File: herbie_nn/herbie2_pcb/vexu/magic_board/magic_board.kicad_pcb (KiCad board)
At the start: 2 copper layers, 70 x 50 mm, 65 parts, among them J1 4P4C, J2 Conn_ARM_JTAG_SWD_10, J3 USB_C_Receptacle_USB2.0_14P, J4 Conn_01x04_Pin, J5 Conn_01x04_Pin, U10 SN74LVC245APW, U11 74HC14, U2 AT25SF081-SSHD-X, U3 BD33FC0WEFJ, U4 ATSAMD51J19A-A, U5 LS7366R, U6 LS7366R, U7 LS7366R, U8 LS7366R, U9 SN74LVC245APW, Y1 32.768KHz, Y2 20MHz

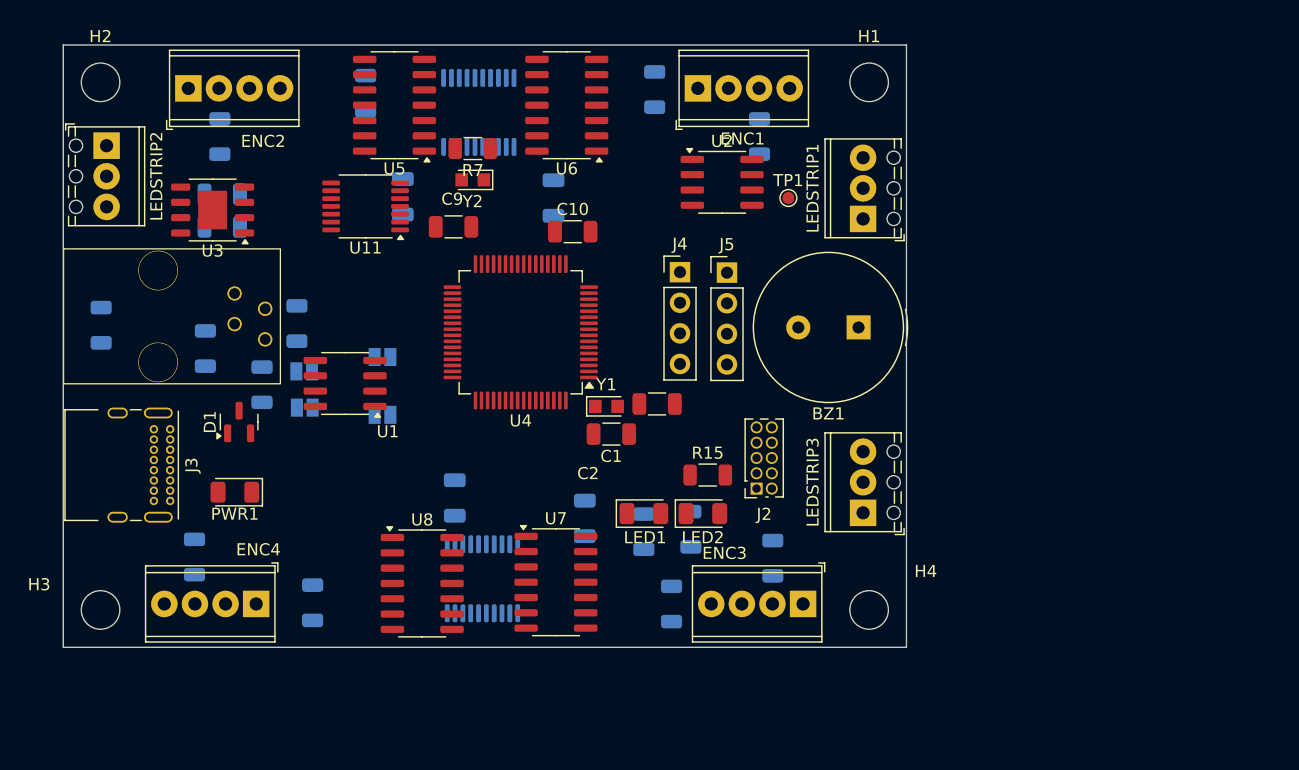
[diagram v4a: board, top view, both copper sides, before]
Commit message: change regulator
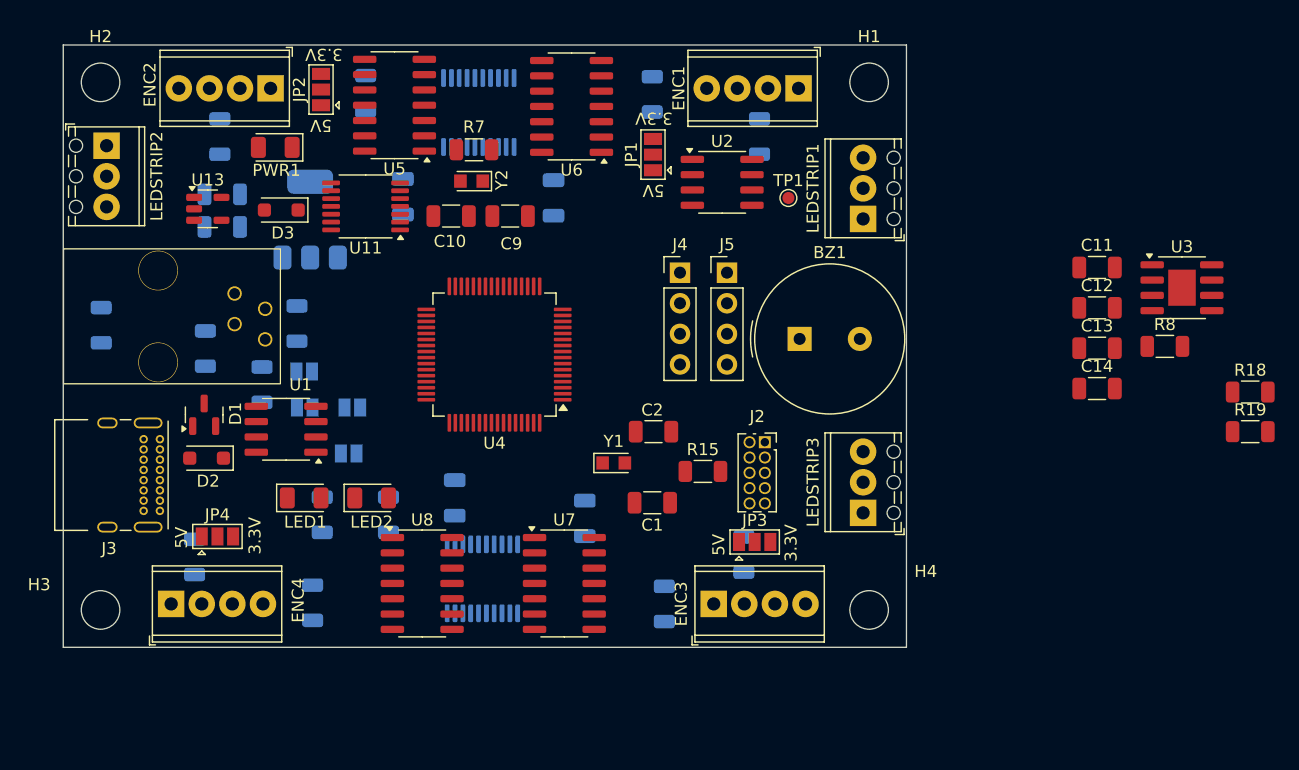
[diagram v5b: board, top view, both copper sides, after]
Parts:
- added C11: C, Capacitor_SMD:C_1206_3216Metric, F.Cu at (111.3, 80.5)
- added C12: C, Capacitor_SMD:C_1206_3216Metric, F.Cu at (111.3, 83.8)
- added C13: C, Capacitor_SMD:C_1206_3216Metric, F.Cu at (111.3, 87.2)
- added C14: C, Capacitor_SMD:C_1206_3216Metric, F.Cu at (111.3, 90.5)
- added D2: MBR1020VL, Diode_SMD:D_SOD-123F, F.Cu at (37.4, 96.3)
- added D3: MBR1020VL, Diode_SMD:D_SOD-123F, F.Cu at (43.6, 75.7)
- added JP1: SolderJumper_3_Open, Jumper:SolderJumper-3_P1.3mm_Open_Pad1.0x1.5mm, F.Cu at (74.5, 71.1)
- added JP2: SolderJumper_3_Open, Jumper:SolderJumper-3_P1.3mm_Open_Pad1.0x1.5mm, F.Cu at (46.9, 65.7)
- added JP3: SolderJumper_3_Open, Jumper:SolderJumper-3_P1.3mm_Open_Pad1.0x1.5mm, F.Cu at (82.9, 103.3)
- added JP4: SolderJumper_3_Open, Jumper:SolderJumper-3_P1.3mm_Open_Pad1.0x1.5mm, F.Cu at (38.3, 102.8)
- added R18: R, Resistor_SMD:R_1206_3216Metric, F.Cu at (124.0, 90.8)
- added R19: R, Resistor_SMD:R_1206_3216Metric, F.Cu at (124.0, 94.1)
- added R8: R, Resistor_SMD:R_1206_3216Metric, F.Cu at (117.0, 87.0)
- added U12: AMS1117-5.0, Package_TO_SOT_SMD:SOT-223-3_TabPin2, B.Cu at (46.0, 76.5)
- added U13: AP2112K-3.3, Package_TO_SOT_SMD:SOT-23-5, F.Cu at (37.5, 75.6)
- U3: value BD33FC0WEFJ -> LM386; footprint Package_SO:HTSOP-8-1EP_3.9x4.9mm_P1.27mm_EP2.4x3.2mm -> Package_SO:SOIC-8-1EP_3.9x4.9mm_P1.27mm_EP2.29x3mm
- Y2: value 20MHz -> 8MHz
- moved U3 80.7 mm to (118.4, 82.2), turned to 0 degrees
- moved PWR1 28.8 mm to (43.1, 70.5)
- moved LED1 28.2 mm to (45.5, 99.6)
- moved LED2 27.5 mm to (51.1, 99.6)
- moved R4 26.7 mm to (47.0, 101.0)
- moved R5 25.1 mm to (52.5, 101.0)
- moved C10 10.2 mm to (57.7, 76.2)
- moved ENC1 8.36 mm to (86.5, 65.6), turned to 180 degrees
- moved ENC3 7.42 mm to (79.5, 108.4), turned to 0 degrees
- moved ENC4 7.05 mm to (34.5, 108.4), turned to 0 degrees
- moved ENC2 6.83 mm to (42.7, 65.6), turned to 180 degrees
- moved C1 6.64 mm to (74.4, 100.0)
- moved U1 6.20 mm to (44.0, 93.9)
- moved BZ1 4.98 mm to (86.6, 86.4), turned to 0 degrees
- moved JP_TX1 4.89 mm to (49.5, 92.1), turned to 180 degrees
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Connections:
- ENC1 pad 4: unconnected-(ENC1-Pin_4-Pad4) -> Net-(ENC1-Pin_4)
- ENC2 pad 4: unconnected-(ENC2-Pin_4-Pad4) -> Net-(ENC2-Pin_4)
- ENC3 pad 4: unconnected-(ENC3-Pin_4-Pad4) -> Net-(ENC3-Pin_4)
- ENC4 pad 4: unconnected-(ENC4-Pin_4-Pad4) -> Net-(ENC4-Pin_4)
- R3 pad 1: +12V -> +5V
- U3 pad 1: +3.3V -> Net-(C13-Pad1)
- U3 pad 2: unconnected-(U3-NC-Pad2) -> GND
- U3 pad 3: GND -> Net-(U3-+)
- U3 pad 4: unconnected-(U3-NC-Pad4) -> GND
- U3 pad 5: +12V -> Net-(C11-Pad1)
- U3 pad 6: unconnected-(U3-NC-Pad6) -> +5V
- U3 pad 8: +12V -> Net-(C13-Pad2)
- U3 pad 9: GND -> (no net)
- U9 pad 1: unconnected-(U9-DIR-Pad1) -> +3.3V
- U9 pad 19: unconnected-(U9-~{OE}-Pad19) -> GND
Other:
- board text added: "3.3V"
- board text added: "5V"

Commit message: updated encoder chip
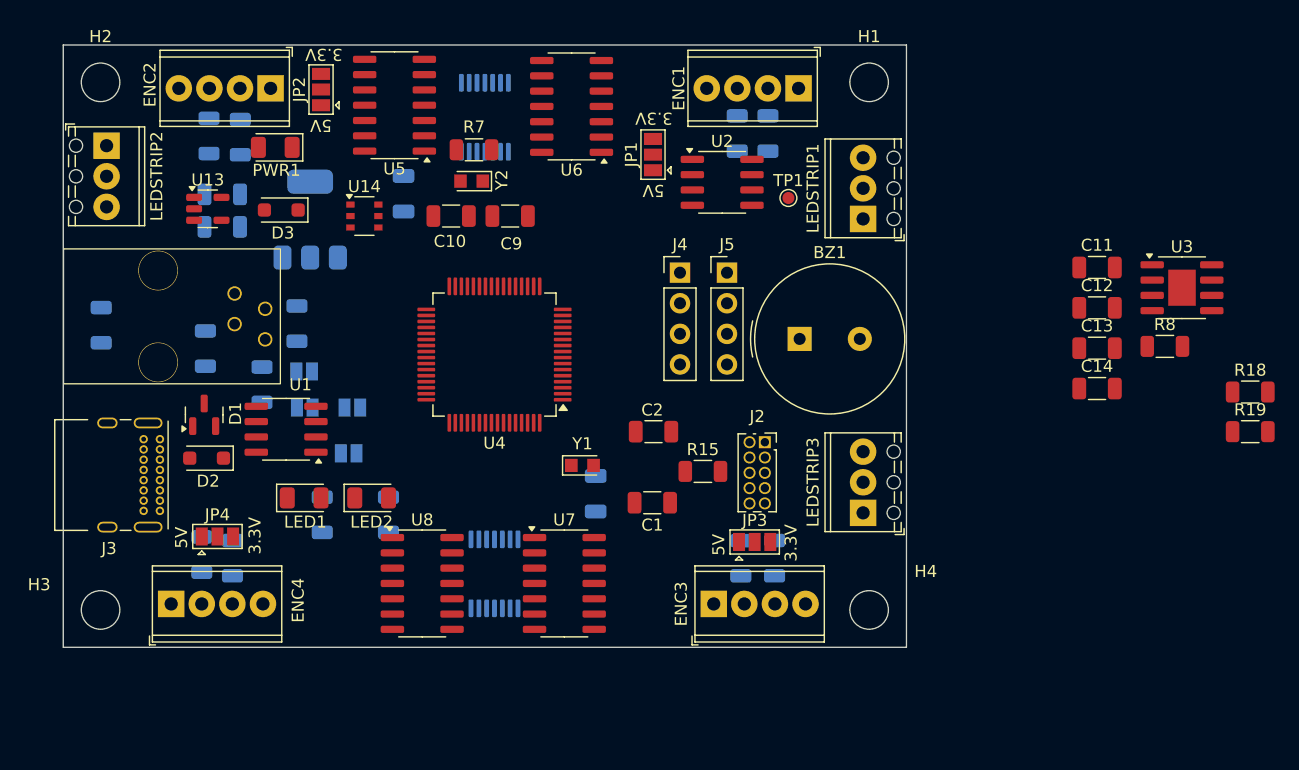
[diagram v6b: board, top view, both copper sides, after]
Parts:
- removed C4, C5: C, Capacitor_SMD:C_1206_3216Metric
- removed R10, R11, R12, R13, R14, R16, R17, R9: R, Resistor_SMD:R_1206_3216Metric
- removed U10, U9: SN74LVC245APW, Package_SO:TSSOP-20_4.4x6.5mm_P0.65mm
- added R20: R, Resistor_SMD:R_1206_3216Metric, B.Cu at (84.0, 69.3)
- added R21: R, Resistor_SMD:R_1206_3216Metric, B.Cu at (81.5, 69.3)
- added R22: R, Resistor_SMD:R_1206_3216Metric, B.Cu at (40.2, 69.7)
- added R23: R, Resistor_SMD:R_1206_3216Metric, B.Cu at (37.6, 69.5)
- added R24: R, Resistor_SMD:R_1206_3216Metric, B.Cu at (81.8, 104.6)
- added R25: R, Resistor_SMD:R_1206_3216Metric, B.Cu at (84.5, 104.6)
- added R26: R, Resistor_SMD:R_1206_3216Metric, B.Cu at (37.0, 104.3)
- added R27: R, Resistor_SMD:R_1206_3216Metric, B.Cu at (39.5, 104.6)
- added U14: 74LVC2G14, Package_SO:TSOP-6_1.65x3.05mm_P0.95mm, F.Cu at (50.5, 76.2)
- added U15: 74LVC125, Package_SO:TSSOP-14_4.4x5mm_P0.65mm, B.Cu at (61.3, 105.9)
- U11: value 74HC14 -> 74LVC125; moved to B.Cu
- moved U11 12.4 mm to (60.5, 68.0), turned to 90 degrees
- moved C6 11.7 mm to (69.7, 99.2)
- moved Y1 2.61 mm to (68.6, 96.9)
- moved C3 0.25 mm to (53.8, 74.3)
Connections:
- U11 pad 1: /EN_CLK -> GND
- U11 pad 10: (no net) -> GND
- U11 pad 11: (no net) -> /B2
- U11 pad 12: (no net) -> Net-(R23-Pad2)
- U11 pad 13: (no net) -> GND
- U11 pad 14: (no net) -> +3.3V
- U11 pad 2: /OUT_CLK -> Net-(R20-Pad2)
- U11 pad 3: unconnected-(U11-Pad3) -> /A1
- U11 pad 4: unconnected-(U11-Pad4) -> GND
- U11 pad 5: unconnected-(U11-Pad5) -> Net-(R21-Pad2)
- U11 pad 6: unconnected-(U11-Pad6) -> /B1
- U11 pad 7: (no net) -> GND
- U11 pad 8: (no net) -> /A2
- U11 pad 9: (no net) -> Net-(R22-Pad2)

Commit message: added labels and logo
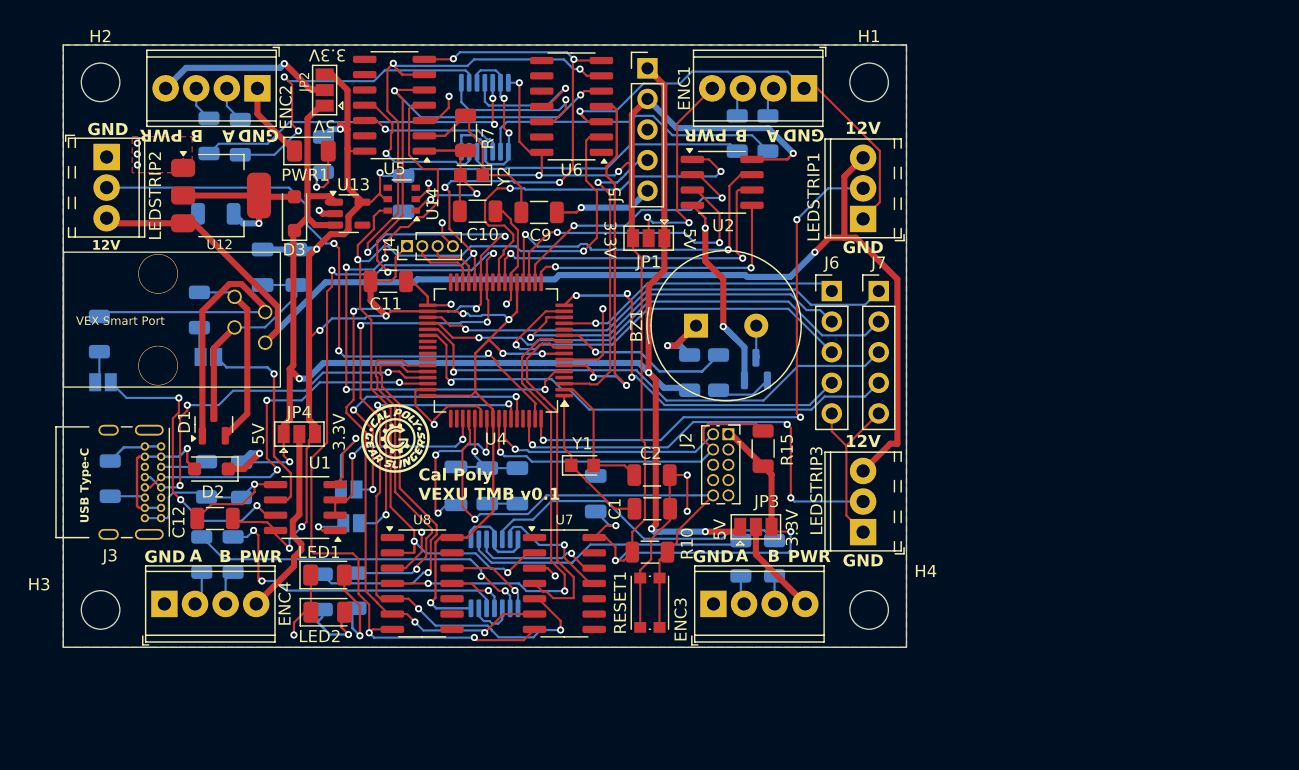
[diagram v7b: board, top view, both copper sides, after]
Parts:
- removed C14: C, Capacitor_SMD:C_1206_3216Metric
- removed R18, R19, R8: R, Resistor_SMD:R_1206_3216Metric
- removed TP1: TestPoint, TestPoint:TestPoint_Pad_D1.0mm
- removed U3: LM386, Package_SO:SOIC-8-1EP_3.9x4.9mm_P1.27mm_EP2.29x3mm
- added C4: 1uF, Capacitor_SMD:C_1206_3216Metric, B.Cu at (60.7, 98.6)
- added C5: 10uF, Capacitor_SMD:C_1206_3216Metric, B.Cu at (63.2, 98.6)
- added G***: LOGO, js_magic_board:logo.mod, F.Cu at (53.1, 94.7)
- added J6: Conn_01x05_Pin, Connector_PinHeader_2.54mm:PinHeader_1x05_P2.54mm_Vertical, F.Cu at (89.3, 82.4)
- added J7: Conn_01x05_Pin, Connector_PinHeader_2.54mm:PinHeader_1x05_P2.54mm_Vertical, F.Cu at (93.2, 82.4)
- added L1: 10uH, Inductor_SMD:L_1206_3216Metric, B.Cu at (58.1, 98.6)
- added Q2: MMBT3904, Package_TO_SOT_SMD:SOT-23, B.Cu at (83.0, 88.9)
- added R10: R, Resistor_SMD:R_1206_3216Metric, F.Cu at (74.2, 104.1)
- added R11: 5.1K, Resistor_SMD:R_1206_3216Metric, B.Cu at (29.4, 98.0)
- added R12: 1K, Resistor_SMD:R_1206_3216Metric, B.Cu at (79.9, 89.2)
- added R13: R, Resistor_SMD:R_1206_3216Metric, B.Cu at (77.5, 89.2)
- added R9: 5.1K, Resistor_SMD:R_1206_3216Metric, B.Cu at (37.4, 98.0)
- added RESET1: SW_SPST, Button_Switch_SMD:SW_Push_1P1T_NO_CK_KMR2, F.Cu at (74.2, 108.3)
- C10, C9: value C -> 12pF
- C11, C12, C3, C6: value C -> .1uF
- C13: value C -> 22uF; moved to B.Cu
- J4: value Conn_01x04_Pin -> Conn_01x04_Socket; footprint Connector_PinHeader_2.54mm:PinHeader_1x04_P2.54mm_Vertical -> Connector_PinHeader_1.27mm:PinHeader_1x04_P1.27mm_Vertical
- J5: value Conn_01x04_Pin -> Conn_01x05_Pin; footprint Connector_PinHeader_2.54mm:PinHeader_1x04_P2.54mm_Vertical -> Connector_PinHeader_2.54mm:PinHeader_1x05_P2.54mm_Vertical
- LEDSTRIP1, LEDSTRIP2, LEDSTRIP3: footprint TerminalBlock_Phoenix:TerminalBlock_Phoenix_MPT-0,5-3-2.54_1x03_P2.54mm_Horizontal -> js_magic_board:TerminalBlock_Phoenix_MPT-0,5-3-2.54_1x03_P2.54mm_Horizontal
- U12: moved to F.Cu
- moved C12 75.3 mm to (38.1, 101.3), turned to 180 degrees
- moved C13 74.0 mm to (38.2, 76.0), turned to 180 degrees
- moved C11 58.9 mm to (52.5, 81.6)
- moved R6 23.3 mm to (47.1, 71.1)
- moved J4 22.8 mm to (54.0, 78.7), turned to 90 degrees
- moved J5 18.2 mm to (74.0, 63.9)
- moved JP_D-1 16.7 mm to (28.8, 90.0)
- moved R2 16.4 mm to (28.5, 86.0)
- moved U13 11.7 mm to (49.2, 76.0)
- moved JP4 10.9 mm to (45.1, 94.3)
- moved LED2 10.2 mm to (47.5, 109.1)
- moved JP_D+1 9.04 mm to (37.5, 87.9)
- moved BZ1 8.67 mm to (78.0, 85.3)
- moved R5 8.44 mm to (47.0, 107.4)
- moved R3 8.08 mm to (40.3, 98.1)
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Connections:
- BZ1 pad 1: /BUZ_PIN -> Net-(BZ1-+)
- BZ1 pad 2: GND -> Net-(BZ1--)
- C11 pad 1: Net-(C11-Pad1) -> +3.3V
- C11 pad 2: unconnected-(C11-Pad2) -> GND
- C12 pad 1: Net-(C11-Pad1) -> +3.3V
- C12 pad 2: Net-(C12-Pad2) -> GND
- C13 pad 1: Net-(C13-Pad1) -> Net-(D3-A)
- C13 pad 2: Net-(C13-Pad2) -> GND
- ENC1 pad 1: unconnected-(ENC1-Pin_1-Pad1) -> GND
- ENC2 pad 1: unconnected-(ENC2-Pin_1-Pad1) -> GND
- ENC3 pad 1: unconnected-(ENC3-Pin_1-Pad1) -> GND
- ENC4 pad 1: unconnected-(ENC4-Pin_1-Pad1) -> GND
- J1 pad 1: /DATA+ -> /DATA-
- J1 pad 2: /DATA- -> /DATA+
- J3 pad A5: unconnected-(J3-CC1-PadA5) -> Net-(J3-CC1)
- J3 pad B5: unconnected-(J3-CC2-PadB5) -> Net-(J3-CC2)
- J4 pad 1: unconnected-(J4-Pin_1-Pad1) -> +3.3V
- J4 pad 2: unconnected-(J4-Pin_2-Pad2) -> /SCL
- J4 pad 3: unconnected-(J4-Pin_3-Pad3) -> /SDA
- J4 pad 4: unconnected-(J4-Pin_4-Pad4) -> GND
- J5 pad 1: unconnected-(J5-Pin_1-Pad1) -> +5V
- J5 pad 2: unconnected-(J5-Pin_2-Pad2) -> +3.3V
- J5 pad 3: unconnected-(J5-Pin_3-Pad3) -> /PA_03
- J5 pad 4: unconnected-(J5-Pin_4-Pad4) -> /DAC_OUT0
- R1 pad 2: /DATA+ -> /DATA-
- R2 pad 2: /DATA- -> /DATA+
- R4 pad 2: unconnected-(R4-Pad2) -> /LED1_PIN
- R5 pad 2: unconnected-(R5-Pad2) -> /LED2_PIN
- U4 pad 4: unconnected-(U4-PA03-Pad4) -> /PA03
- U4 pad 43: unconnected-(U4-PA22-Pad43) -> /LED1_PIN
- U4 pad 44: unconnected-(U4-PA23-Pad44) -> /LED2_PIN
- U4 pad 53: unconnected-(U4-VDDCORE-Pad53) -> Net-(U4-VDDCORE)
- U4 pad 55: unconnected-(U4-VSW-Pad55) -> Net-(U4-VSW)
- U4 pad 8: unconnected-(U4-VDDANA-Pad8) -> +3.3V
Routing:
- net +3.3V: track 0.00 -> 263.3 mm, vias 0 -> 19
- net GND: track 0.00 -> 232.6 mm, vias 0 -> 23
- net +5V: track 0.00 -> 128.6 mm, vias 0 -> 6
- net /MISO: track 0.00 -> 110.1 mm, vias 0 -> 8
- net /MOSI: track 0.00 -> 108.4 mm, vias 0 -> 8
- net /SCK: track 0.00 -> 108.0 mm, vias 0 -> 8
- net +12V: track 0.00 -> 103.0 mm, vias 0 -> 1
- net /OUT_CLK: track 0.00 -> 77.8 mm, vias 0 -> 4
- net /ENC1_SS: track 0.00 -> 50.9 mm, vias 0 -> 4
- net /LED_SIG2: track 0.00 -> 50.6 mm, vias 0 -> 3
- net /LED_SIG1: track 0.00 -> 47.2 mm, vias 0 -> 3
- net /SERCOM1.2: track 0.00 -> 43.0 mm, vias 0 -> 1
- net /SERCOM1.3: track 0.00 -> 42.7 mm, vias 0 -> 1
- net /NRESET: track 0.00 -> 42.5 mm, vias 0 -> 1
- net /SERCOM1.1: track 0.00 -> 41.3 mm, vias 0 -> 1
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- added copper zone on B.Cu, net GND
- added copper zone on F.Cu, net GND
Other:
- board text added: "12V"
- board text added: "A"
- board text added: "B"
- board text added: "Cal Poly VEXU TMB v0.1"
- board text added: "GND"
- board text added: "PWR"
- board text added: "USB Type-C"
- board text added: "VEX Smart Port"

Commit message: version 0.1 sent for fabrication
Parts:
- added F1: 500mA, Fuse:Fuse_1206_3216Metric, B.Cu at (38.5, 94.0)
- added R14: 1K, Resistor_SMD:R_1206_3216Metric, B.Cu at (80.8, 81.1)
- added R8: 10K, Resistor_SMD:R_1206_3216Metric, B.Cu at (83.7, 73.4)
- R10: value R -> 10K
- R20, R21, R22, R23, R24, R25, R26, R27: value R -> 100
- moved Q2 0.62 mm to (83.2, 89.5)
- moved G*** 0.11 mm to (53.2, 94.7)
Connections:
- J2 pad 9: unconnected-(J2-GNDDetect-Pad9) -> GND
- J3 pad A4: Net-(D2-A) -> Net-(F1-Pad1)
- J3 pad A9: Net-(D2-A) -> Net-(F1-Pad1)
- J3 pad B4: Net-(D2-A) -> Net-(F1-Pad1)
- J3 pad B9: Net-(D2-A) -> Net-(F1-Pad1)
- U4 pad 4: /PA03 -> /PA_03
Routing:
- net /PA_03: track 0.00 -> 33.5 mm, vias 0 -> 5
- net Net-(F1-Pad1): track 0.00 -> 15.3 mm
- net Net-(BZ1--): track 2.77 -> 14.0 mm, vias 0 -> 2
- net +3.3V: track 263.3 -> 271.6 mm
- net Net-(D2-A): track 12.5 -> 4.31 mm
- net Net-(BZ1-+): track 5.95 -> 11.4 mm, vias 1 -> 2
- net /QSPI_DATA2: track 24.8 -> 22.4 mm
- net /QSPI_CS: track 32.5 -> 34.9 mm
- net /SERCOM1.1: track 41.3 -> 39.2 mm
- net /ENC2_SS: track 31.7 -> 33.3 mm
- net /DAC_OUT0: track 25.3 -> 26.8 mm
- net /QSPI_DATA0: track 23.7 -> 25.1 mm
- net Net-(JP_D-1-A): track 24.6 -> 23.2 mm
- net +5V: track 128.6 -> 127.4 mm
- net /QSPI_DATA3: track 29.0 -> 27.9 mm
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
